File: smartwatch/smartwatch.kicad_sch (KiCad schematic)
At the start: 35 parts, among them J1 BAT_CON, J2 DC_CON, J3 PROG_INT, J4 SM13B-GHS-TB, SW1 SW_Push, U1 ESP32-WROVER-E, U2 MCP73831-5-OT, U3 MPU-6050, U3 TLV1117-33

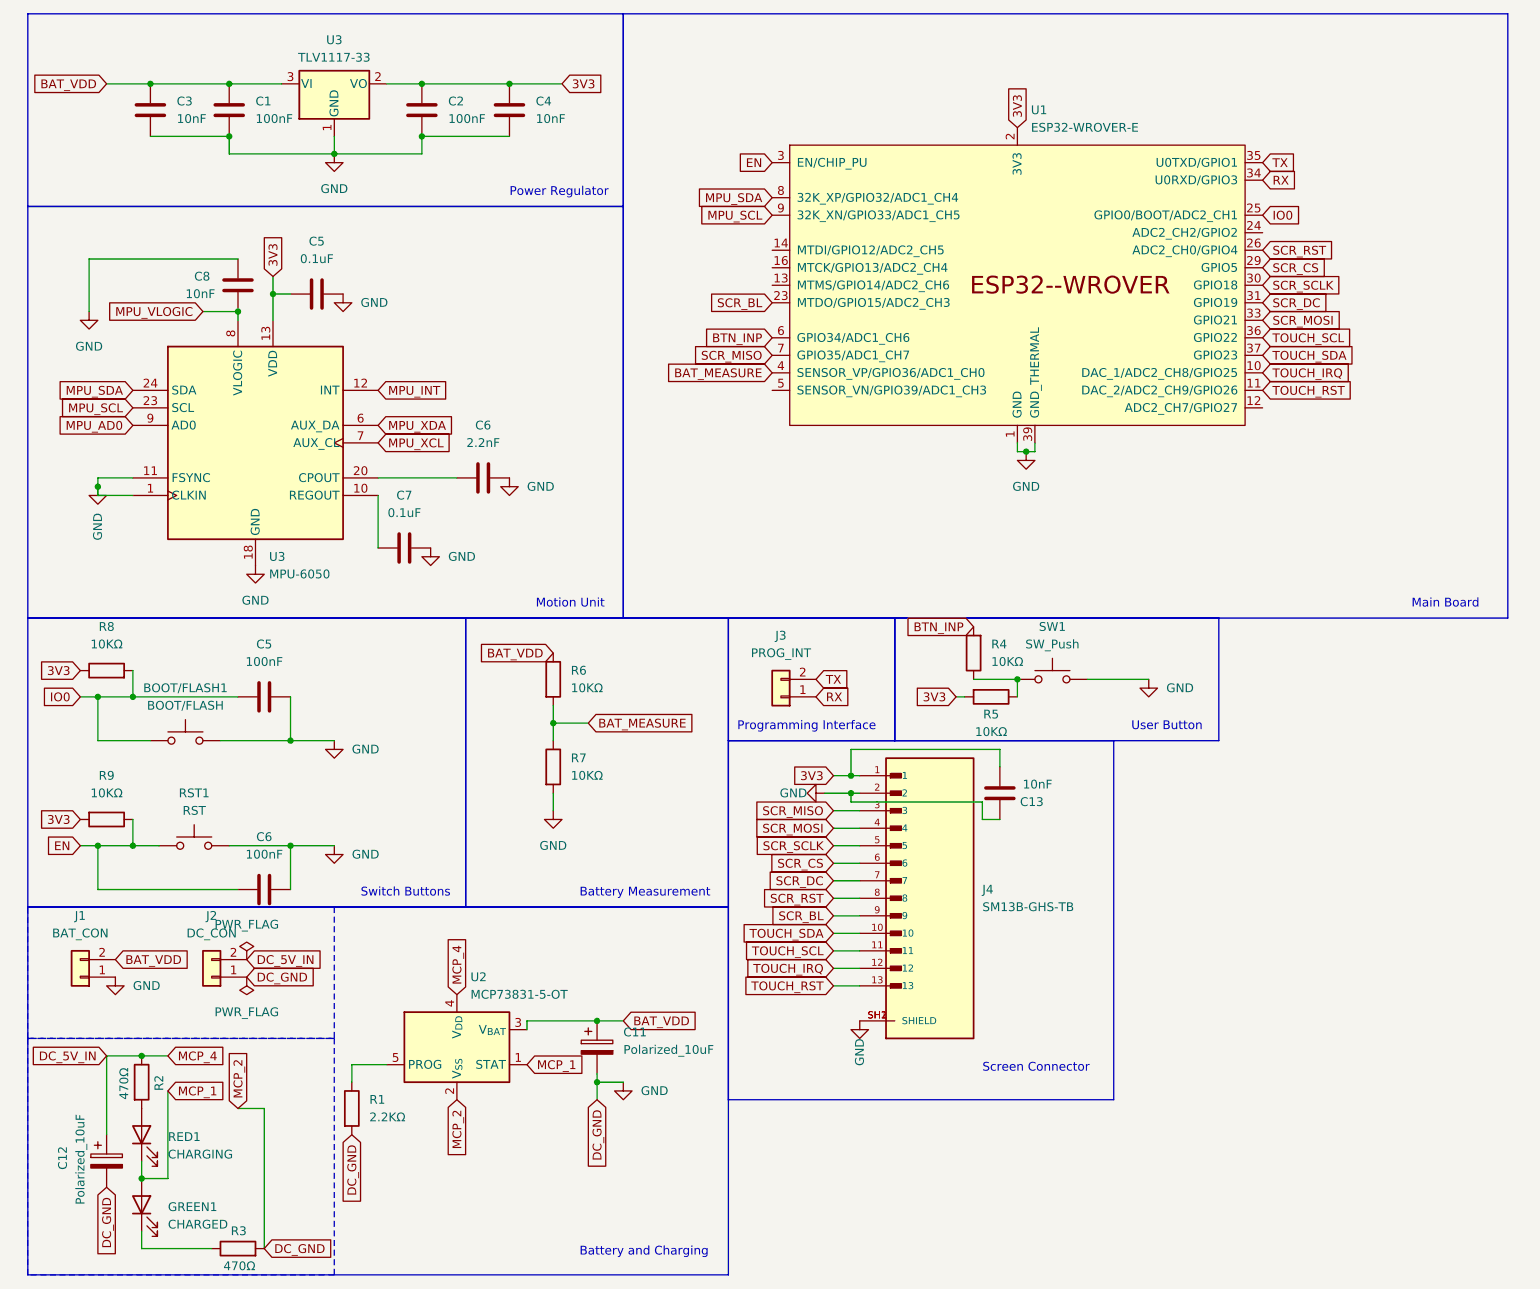
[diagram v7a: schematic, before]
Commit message: added connectors for all and reroute
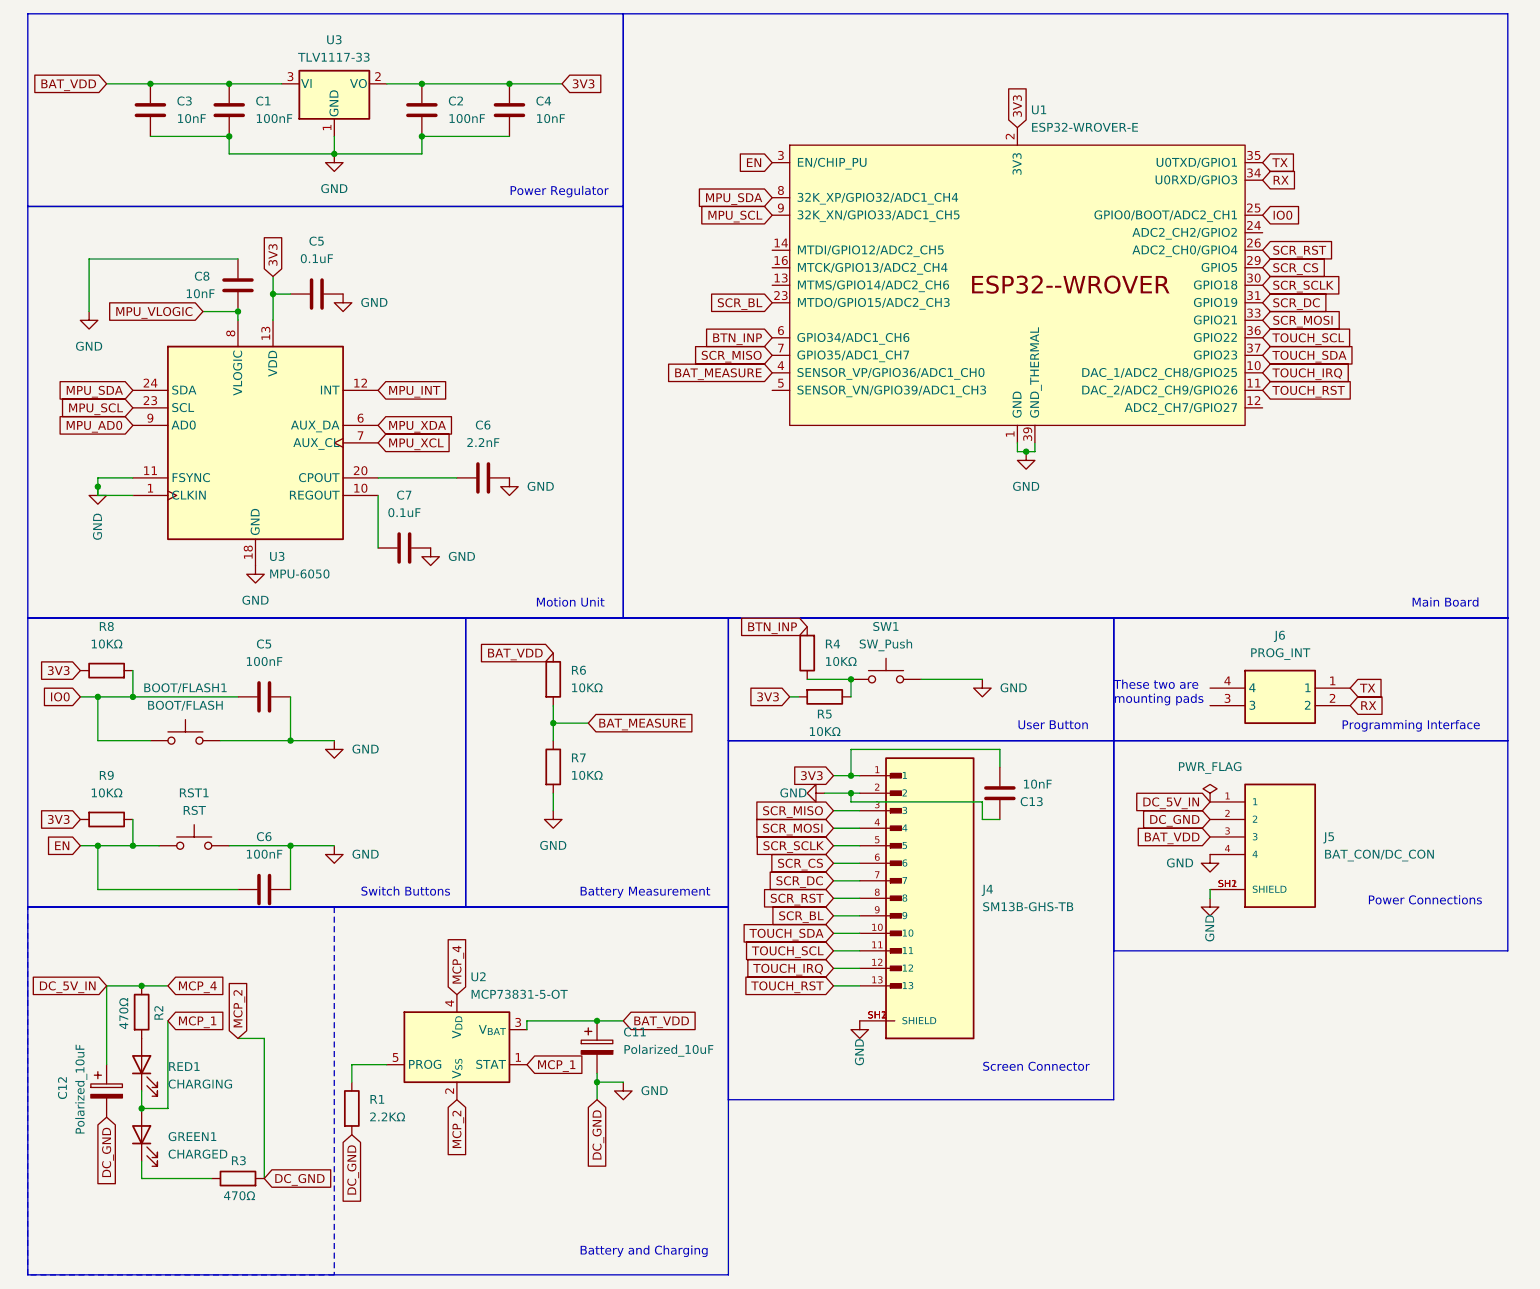
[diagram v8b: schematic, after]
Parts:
- removed J1: BAT_CON, Connector_Wire_SMD:Wire_Pad_1x02, symbol Connector_Generic:Conn_01x02
- removed J2: DC_CON, Connector_Wire_SMD:Wire_Pad_1x02, symbol Connector_Generic:Conn_01x02
- removed J3: PROG_INT, Connector_Wire_SMD:Wire_Pad_1x02, symbol Connector_Generic:Conn_01x02
- added J5: BAT_CON/DC_CON, Connector_JST:JST_GH_SM04B-GHS-TB_1x04-1MP_P1.25mm_Horizontal, symbol SM04B-GHS-TB_LF__SN_-:SM04B-GHS-TB_LF__SN_-
- added J6: PROG_INT, Connector_JST:JST_GH_SM02B-GHS-TB_1x02-1MP_P1.25mm_Horizontal, symbol SM02B-GHS-TB_LF__SN_:SM02B-GHS-TB_LF__SN_
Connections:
- net BAT_VDD: now also J5.3
- net DC_5V_IN: now also J5.1
- net GND: now also J5.2, J5.4, J5.SH1 (SHIELD), J5.SH2 (SHIELD)
- net RX: now also J6.2
- net TX: now also J6.1
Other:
- note added: "Power Connections"
- note added: "These two are mounting pads"
- moved on the sheet: C12, GREEN1, R2, R3, R4, R5, RED1, SW1
